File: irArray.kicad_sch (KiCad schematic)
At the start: 1 part, among them J4 J_VL53L0X

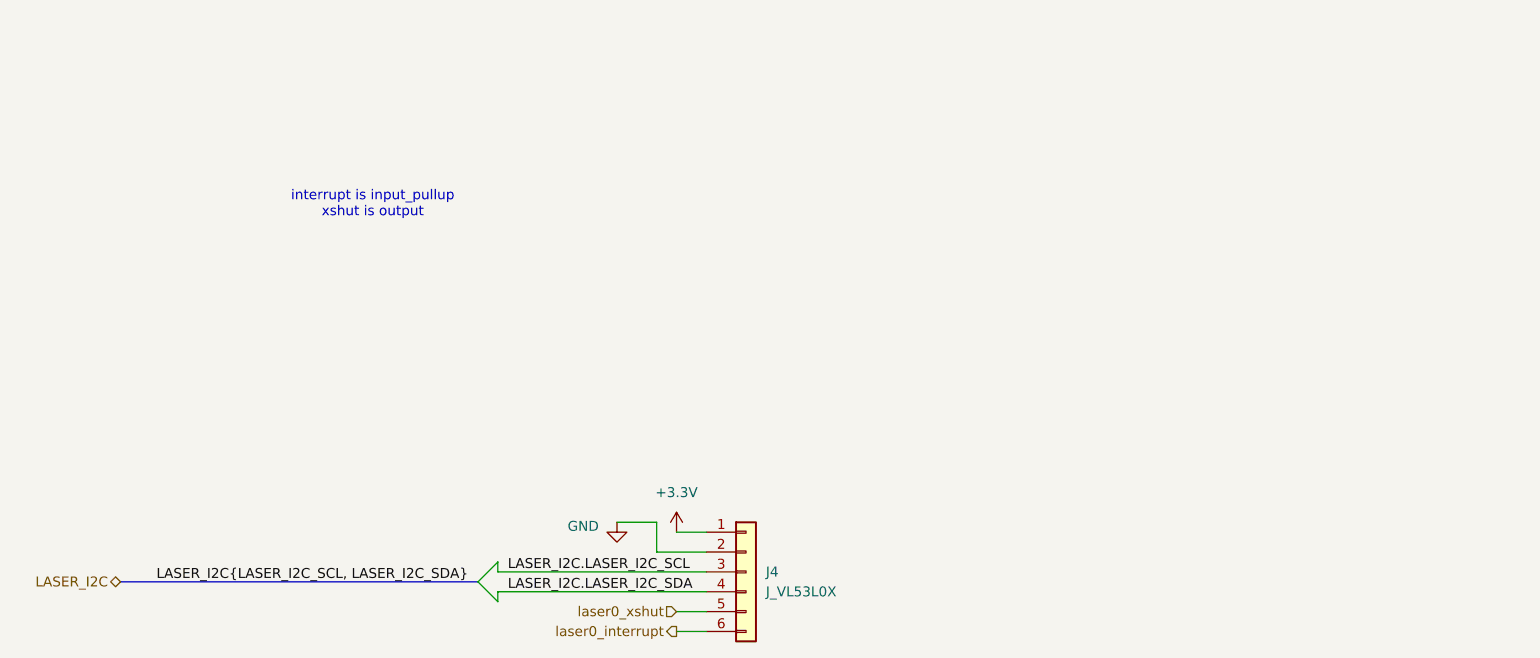
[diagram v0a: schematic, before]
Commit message: added motor controller
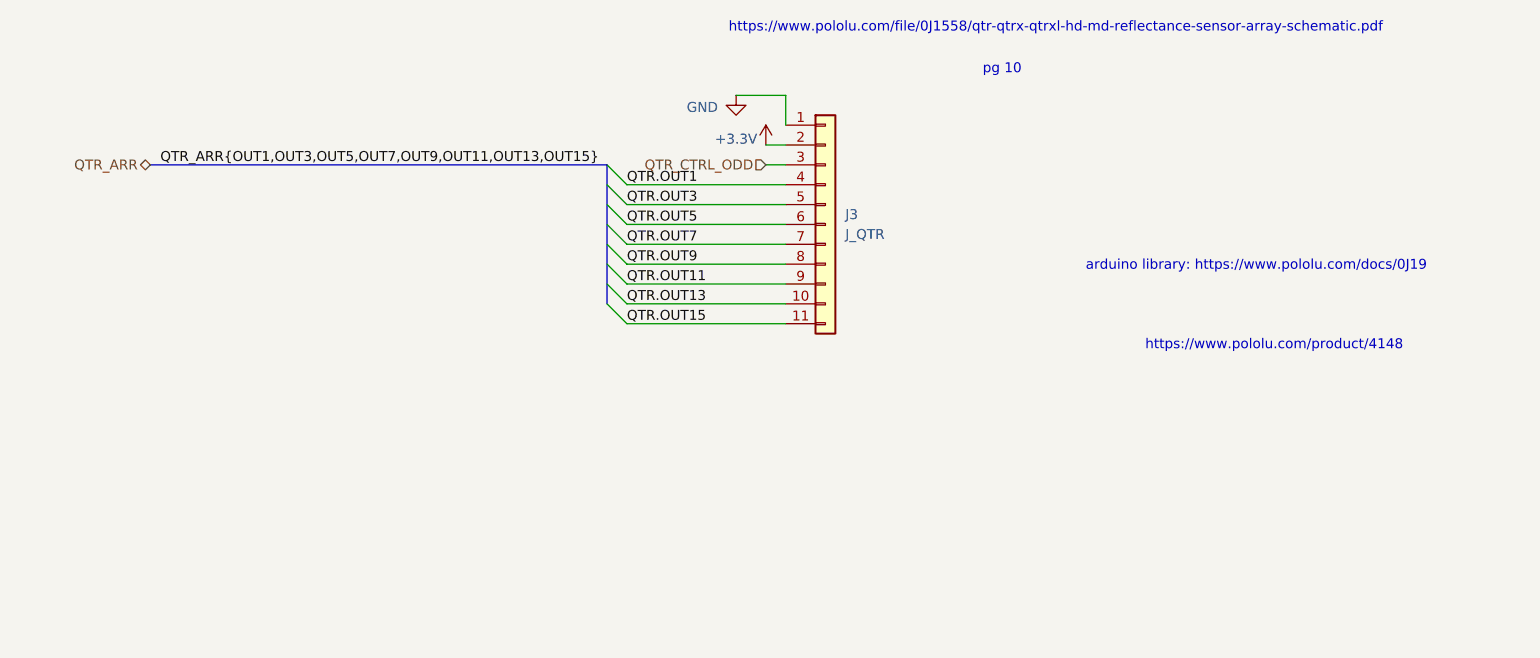
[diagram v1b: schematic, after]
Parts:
- removed J4: J_VL53L0X, Connector_PinHeader_2.54mm:PinHeader_1x06_P2.54mm_Horizontal, symbol Connector_Generic:Conn_01x06
- added J3: J_QTR, symbol Connector_Generic:Conn_01x11
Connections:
- net +3.3V: now also J3.2 (Pin_2)
- net GND: now also J3.1 (Pin_1)
- new net QTR.OUT1: J3.4 (Pin_4)
- new net QTR.OUT11: J3.9 (Pin_9)
- new net QTR.OUT13: J3.10 (Pin_10)
- new net QTR.OUT15: J3.11 (Pin_11)
- new net QTR.OUT3: J3.5 (Pin_5)
- new net QTR.OUT5: J3.6 (Pin_6)
- new net QTR.OUT7: J3.7 (Pin_7)
- new net QTR.OUT9: J3.8 (Pin_8)
- new net QTR_CTRL_ODD: J3.3 (Pin_3)
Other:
- note added: "arduino library: https://www.pololu.com/docs/0J19"
- note added: "https://www.pololu.com/file/0J1558/qtr-qtrx-qtrxl-hd-md-reflectance-sensor-array-schematic.pdf"
- note added: "https://www.pololu.com/product/4148"
- note added: "pg 10"
- note removed: "interrupt is input_pullup xshut is output"
